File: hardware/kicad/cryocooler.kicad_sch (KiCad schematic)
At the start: 16 parts, among them J1 USB_C, SW1 RESET, SW2 BOOT, U1 ESP32-S3-WROOM-2-N32R16V, U2 USBLC6-2SC6

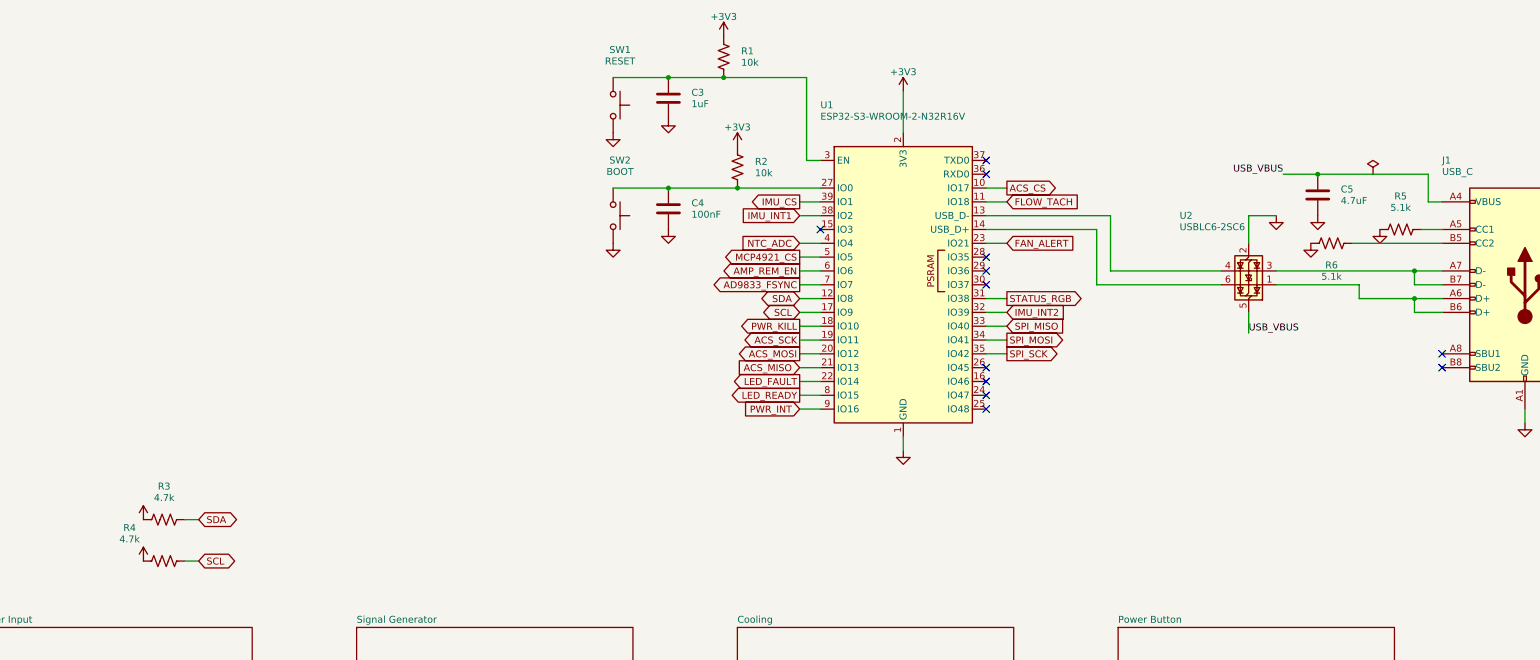
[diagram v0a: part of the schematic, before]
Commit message: Put supply pins on top and grounds on the bottom of IC symbols; flake8-clean Python
Schematic: re-laid out pins on U2, U3, U6, U7, U11, U14, U17-U20, U22-U24
and PS1 (supply on top, ground/strap pins on the bottom edge) via custom
`cryocooler:` symbols (make_lib.from_stock) and a gnd_bus helper; U18/U2
use mirroring instead of a 180 degree rotation. Nets are unchanged (ERC 0,
117/117 datasheet rules, PCB nets still match). Text placement now shows
every power-symbol name, avoids wires, and uses a realistic character width.

Python: black -l 79 -S plus manual wrapping so hardware/kicad and scripts/
pass flake8; add .flake8.

Co-Authored-By: Claude Sonnet 5.5 <noreply@anthropic.com>
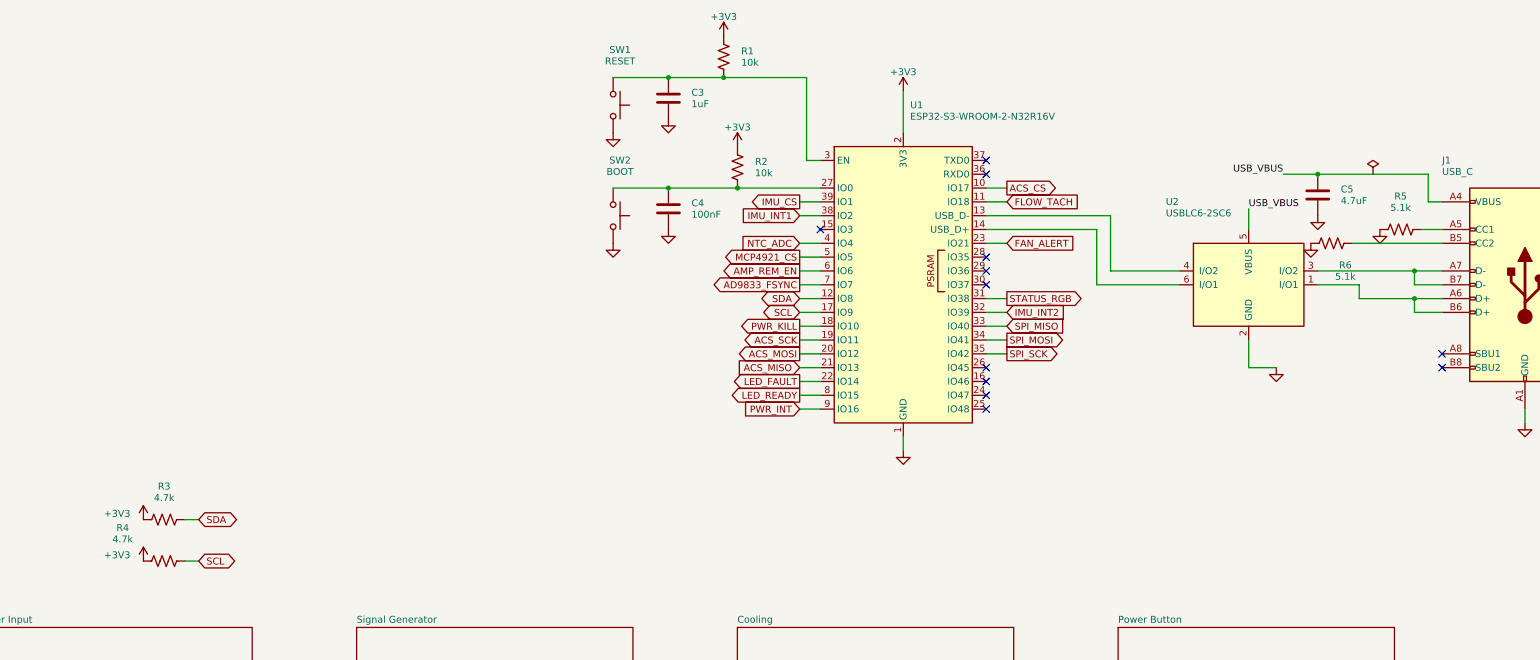
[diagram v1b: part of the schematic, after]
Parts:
- U2: symbol Power_Protection:USBLC6-2SC6 -> cryocooler:USBLC6-2SC6

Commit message: KiCad schematic: INA239, ADS1220, SC18IS604 bridge, relay driver, test points
- system_current: INA237 -> INA239 (SPI, CS GPIO3) with the 49.9 ohm / 470 nF
  input filter, power LED and ALERT LED; VBUS shares the filtered IN- node.
- cold_head: ADS122C04 -> ADS1220 (SPI, CS GPIO44).
- i2c_bridge (new): SC18IS604 SPI-to-I2C bridge for the EMC2303, with a
  74LVC1G125 gating its MISO onto the shared bus.
- compressor_relay (new): GPIO16 high-side switch sharing one generator
  function with the amplifier REM switch.
- debug (new): about 40 test points and rail LEDs (the isolated rail LED
  returns to ISO_GND).
- ISO7741 -> ACS37800 SPI lines are straight wires (pins reordered on the
  symbol); USB_VBUS is one wire plus a naming label.
- Custom symbols for INA239, ADS1220, SC18IS604; datasheet rules 117 -> 162;
  GPIO map checks updated. ERC 0.

Co-Authored-By: Claude Sonnet 5.5 <noreply@anthropic.com>
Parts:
- removed C5: 4.7uF, Capacitor_SMD:C_0805_2012Metric, symbol Device:C
- removed J1: USB_C, Connector_USB:USB_C_Receptacle_GCT_USB4105-xx-A_16P_TopMnt_Horizontal, symbol Connector:USB_C_Receptacle_USB2.0_16P
- removed R5, R6: 5.1k, Resistor_SMD:R_0603_1608Metric, symbol Device:R_US
- added R3, R4: 5.1k, Resistor_SMD:R_0603_1608Metric, symbol Device:R_US
- C5: renamed from R4; value 4.7k -> 4.7uF; footprint Resistor_SMD:R_0603_1608Metric -> Capacitor_SMD:C_0805_2012Metric; symbol Device:R_US -> Device:C
- J1: renamed from R3; value 4.7k -> USB_C; footprint Resistor_SMD:R_0603_1608Metric -> Connector_USB:USB_C_Receptacle_GCT_USB4105-xx-A_16P_TopMnt_Horizontal; symbol Device:R_US -> Connector:USB_C_Receptacle_USB2.0_16P
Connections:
- net +3V3: no longer C5.1, J1.1
- net GND: now also C5.2, J1.A1 (GND), J1.A12 (GND), J1.B1 (GND), J1.B12 (GND), J1.SH (SHIELD), R3.1, R4.1
- net USB_VBUS: now also C5.1, J1.A4 (VBUS), J1.A9 (VBUS), J1.B4 (VBUS), J1.B9 (VBUS)
- net ESP_BOOT: now reaches C4.1, R2.2, SW2.1, U1.27 (IO0)
- net at U2.1 (I/O1): now also J1.A6 (D+), J1.B6 (D+)
- net at U2.3 (I/O2): now also J1.A7 (D-), J1.B7 (D-)
- net ESP_EN: now reaches C3.1, R1.2, SW1.1, U1.3 (EN)
- net INA239_CS: now reaches U1.15 (IO3)
- net ADS1220_CS: now reaches U1.36 (RXD0)
- net UART0_TX: now reaches U1.37 (TXD0)
- net PWR_INT renamed COMP_RELAY_EN
- net SCL renamed BRIDGE_RESET
- net BRIDGE_RESET: no longer C5.2
- net SDA renamed BRIDGE_CS
- net BRIDGE_CS: no longer J1.2
- new net: J1.A5 (CC1), R3.2
- new net: J1.B5 (CC2), R4.2
- no-connect marks 12 -> 9
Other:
- added sheet Compressor Relay (sheets/compressor_relay.kicad_sch)
- added sheet Debug (sheets/debug.kicad_sch)
- added sheet I2C Bridge (sheets/i2c_bridge.kicad_sch)

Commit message: Add per-section supply jumpers, 8-pin IMU header and connector pin labels
- Four 1.27 mm 2-pin jumpers (JP1-JP4), each with a rail-on LED, cut the
  supply of one section for debugging: signal generator +3V3, +-15V
  generator +5V in, isolated amp-current supply +5V in, and a shared
  +3V3 net for the cooling chips (EMC2303, RTD ADC, I2C bridge).
- J14 is now an 8-pin JST XH in the Adafruit LSM6DSOX pad order
  (VIN, GND, SCL, SDA, DO, CS, I1, I2); firmware pin comments updated.
- Pin-function labels beside every connector, "RAILS ±15V" box title.
- Board re-placed and re-routed (130 x 110 mm); DRC 0 errors, 0 unconnected,
  ERC 0, 173 datasheet rules pass. BOM, READMEs, Gerbers and renders
  regenerated; link_usb_vbus.py now adapts to the routed layout.

Co-Authored-By: Claude Sonnet 5.5 <noreply@anthropic.com>
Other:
- added sheet Supply Switches (sheets/supply_switches.kicad_sch)

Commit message: Split cooling into Water Cooling and Cold Head Temp sections, each with a supply jumper and LED
Water Cooling (EMC2303, SC18IS604 bridge, NTC, fan/pump/flow) sits behind JP4
on +3V3_COOL together with its pull-ups. Cold Head Temp (ADS1220, PT1000) gets
a new jumper JP5 and LED D22 on +3V3_CH. JP2 is relabelled for the +-15V rails
and moved into the RAILS +-15V box. PCB regenerated with two silk boxes, routed,
leftovers finished with a grid router; board render added to the main README.

Co-Authored-By: Claude Sonnet 5.5 <noreply@anthropic.com>
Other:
- sheet Cold Head renamed Cold Head Temp
- sheet Cooling renamed Water Cooling
- sheet I2C Bridge renamed Water Cooling I2C Bridge

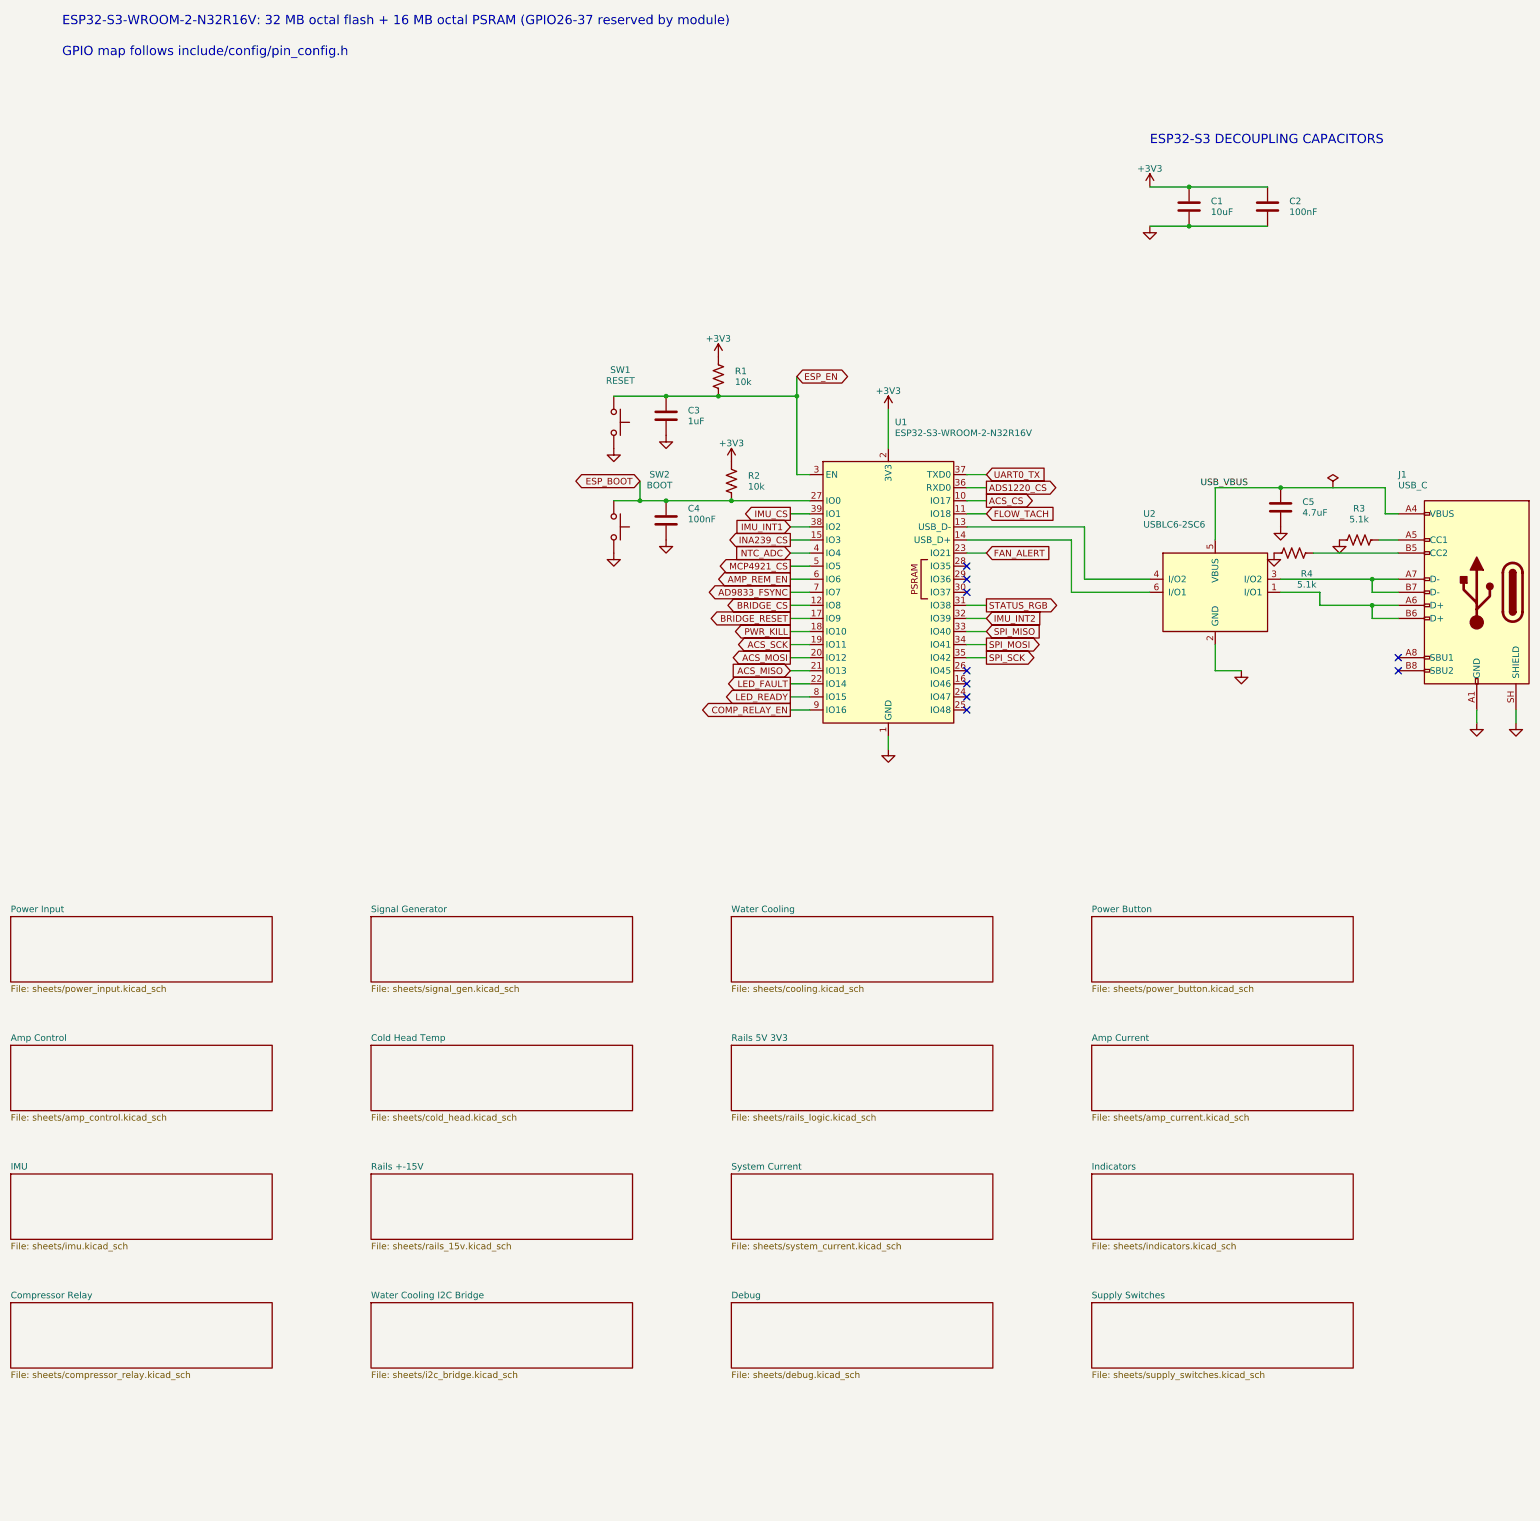
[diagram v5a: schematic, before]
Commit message: Replace the ±15 V LDOs with one LT3097 and add a power-good interlock
- rails_15v: ADP7142 + ADP7182 replaced by one LT3097 (±14.7 V, 147 k SET
  resistors); the ADP5071 output caps are now 22 uF / 50 V and double as the
  LT3097 inputs. PGP / PGN make the PG_15V node (fed from +15 V, so it reads
  0 V if a rail is missing).
- amp_control: a series BSS138 (Q9) gated by PG_15V blocks AMP_REM unless
  both rails are good. New power_good sheet: LED (D23) and the active-low
  PG_15V_N flag on GPIO43 (PG_15V_N_PIN).
- Tooling: LT3097 symbol, footprint and 3D envelope; datasheet rules (191),
  GPIO check, BOM tables, floor plan, PAD_BRIDGES and pre-placed GND vias in
  gen_pcb.py, new fix_route.py for post-route clean-up.
- Board regenerated and routed with Freerouting 2.5.0: DRC 0 unconnected,
  0 schematic-parity issues, no copper violations. Gerbers, JLCPCB zip,
  renders, BOM, CPL and schematic PDF regenerated.

Co-Authored-By: Claude Sonnet 5.5 <noreply@anthropic.com>
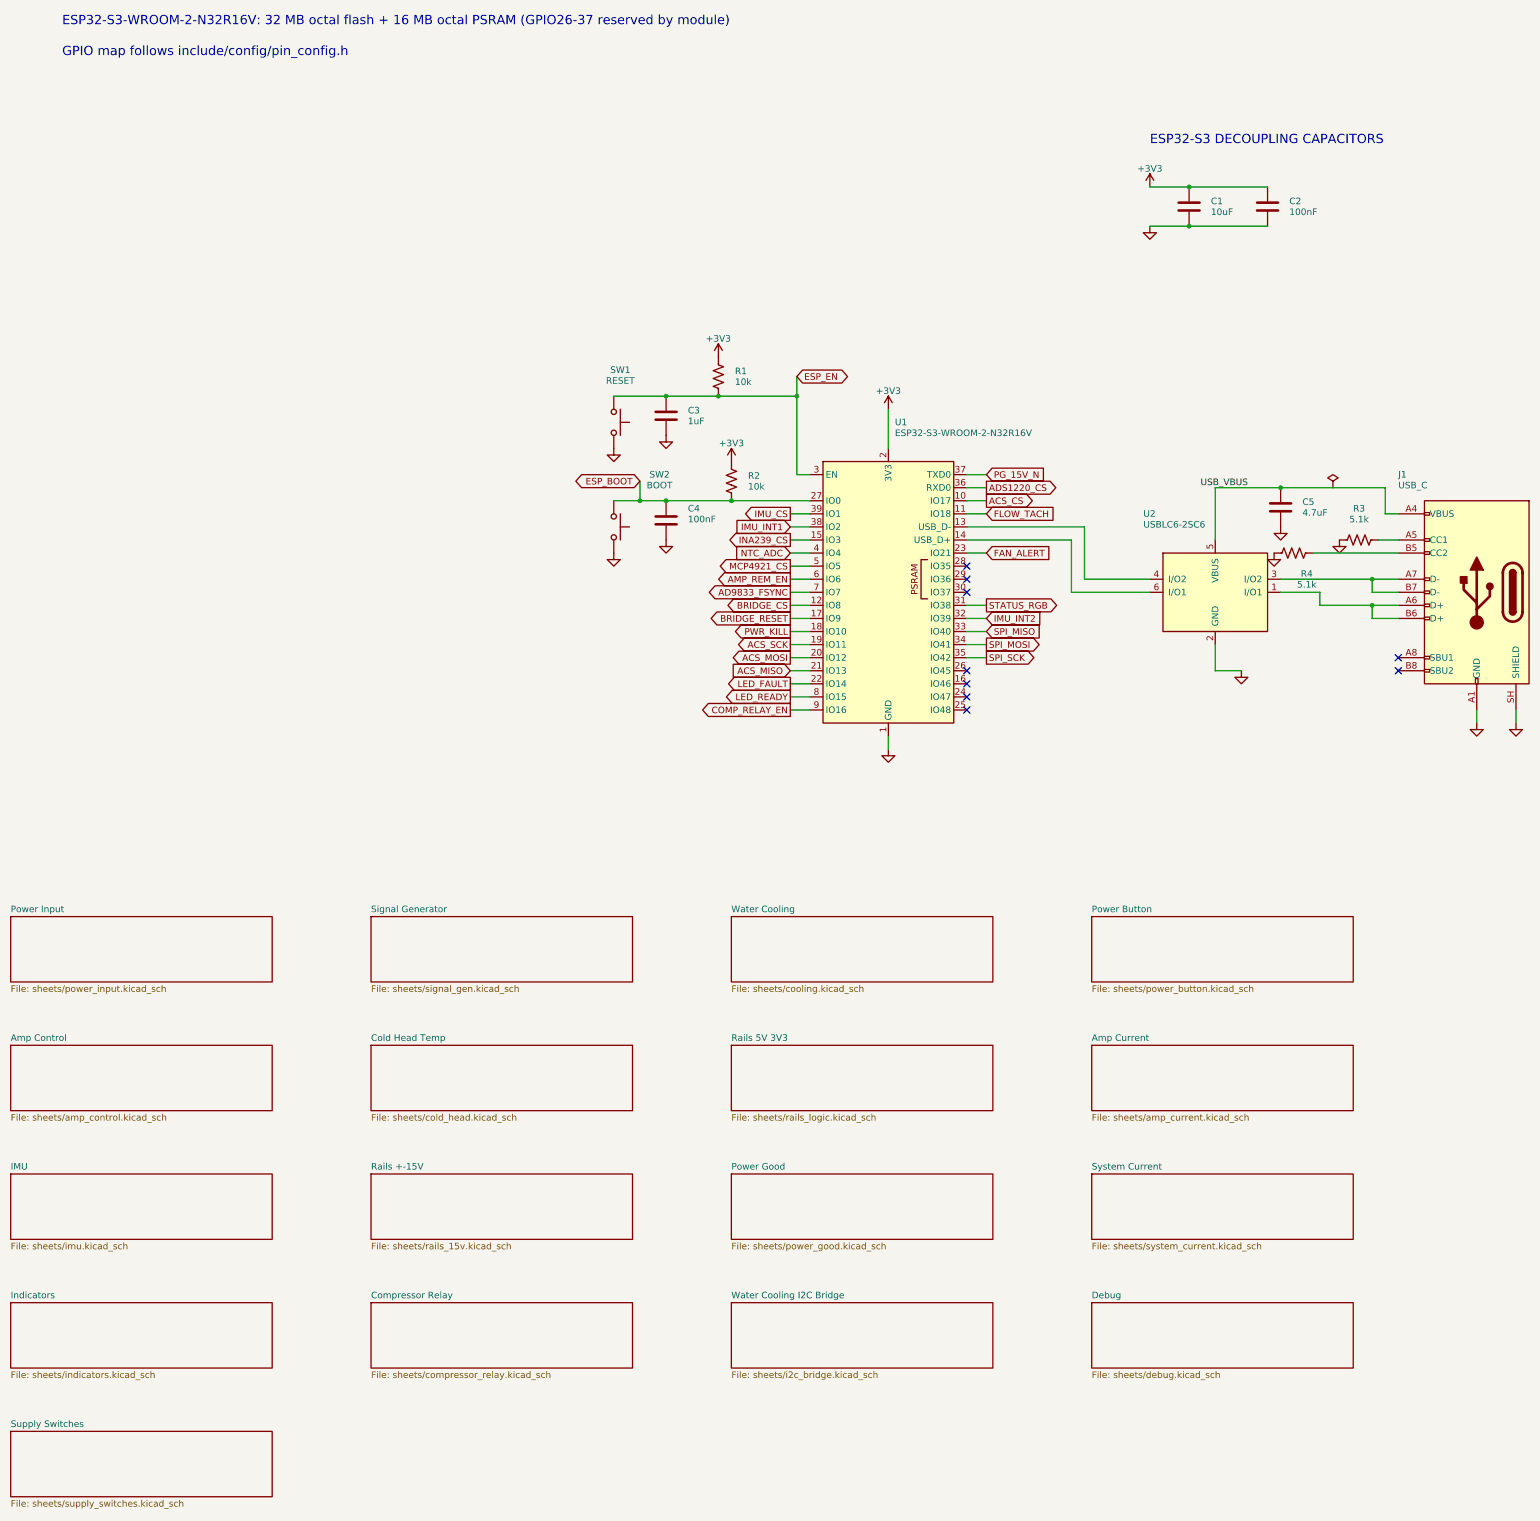
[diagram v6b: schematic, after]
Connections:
- net UART0_TX renamed PG_15V_N
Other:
- added sheet Power Good (sheets/power_good.kicad_sch)
